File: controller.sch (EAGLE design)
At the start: 37 parts, among them IC1 7805DT, Q1 MOSFET_PCHANNEL, Q2 MOSFET-NCHANNELBSS123LT1G, Q3 MOSFET-NCHANNELFDD8780, U1 ATMEGA328P, Y1 16MHz

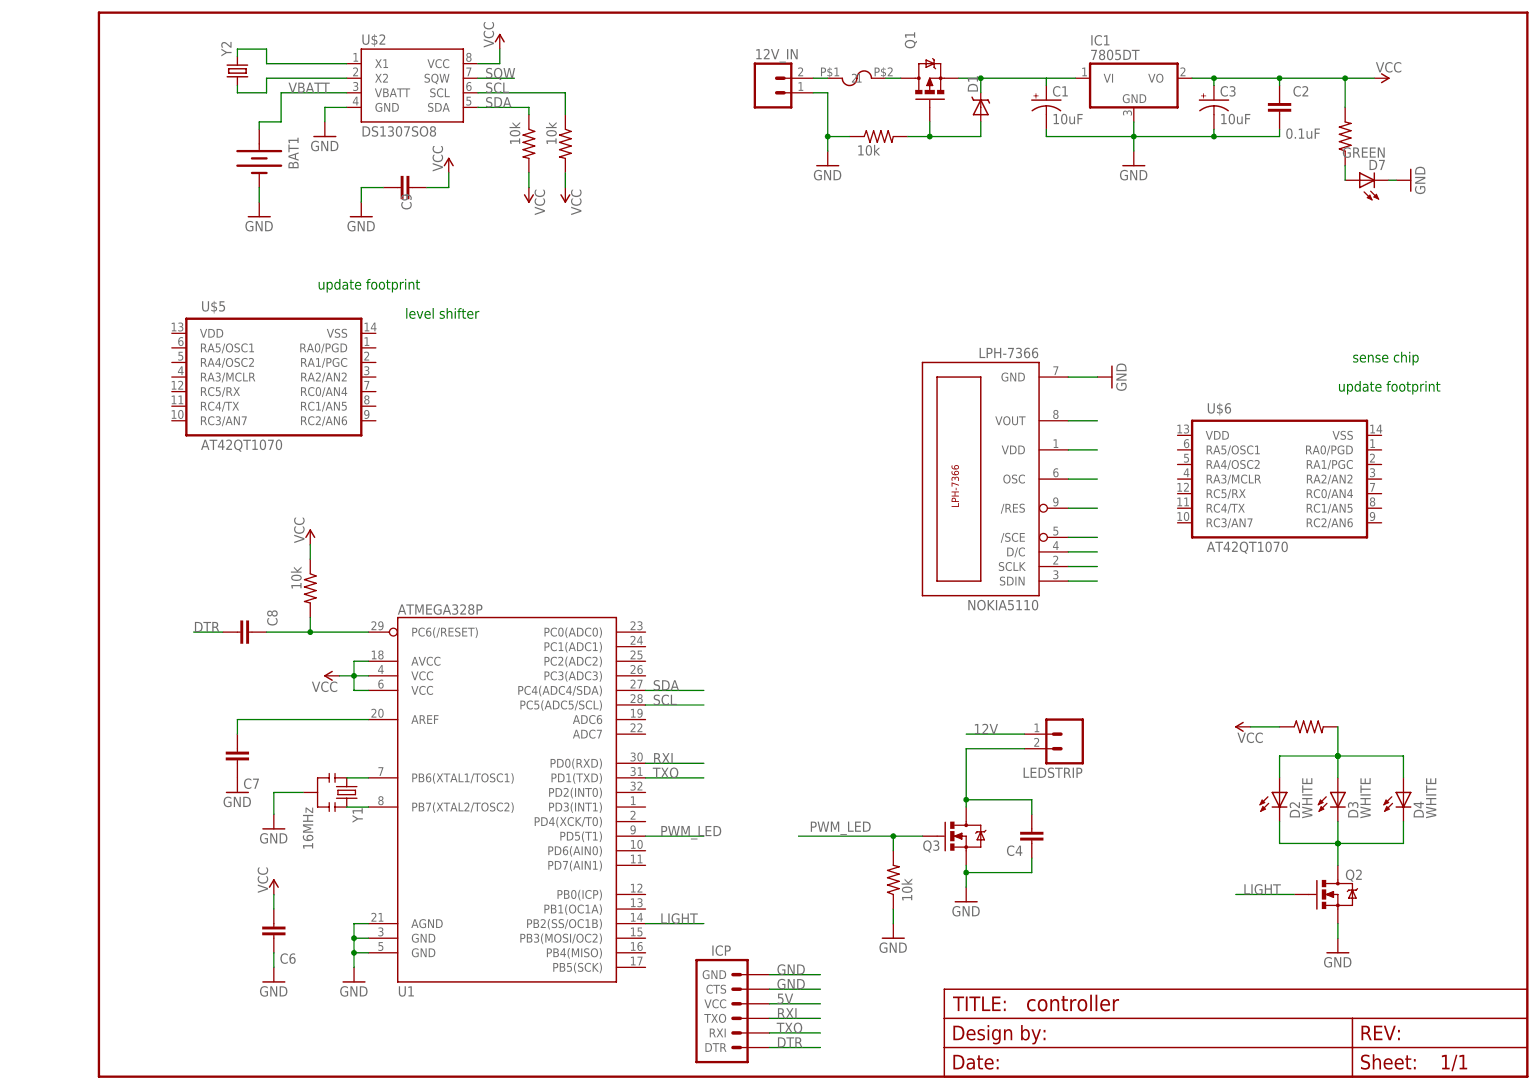
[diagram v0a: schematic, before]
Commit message: added sense IC footprint and jumper. layed out "high" power section.
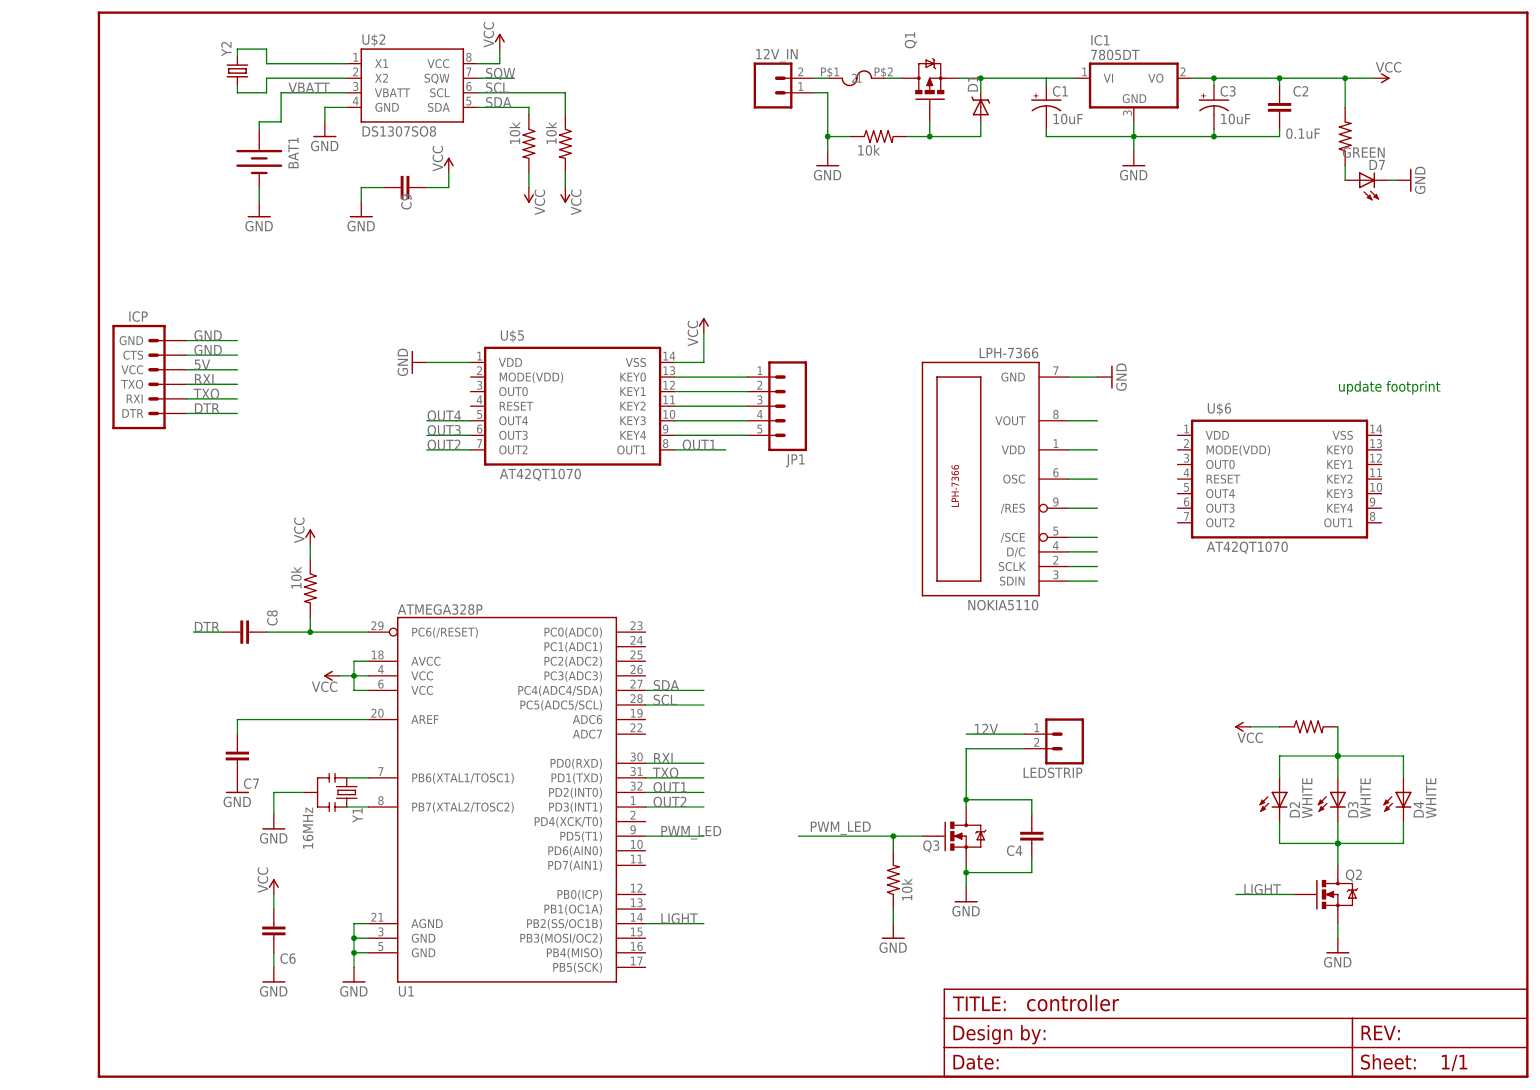
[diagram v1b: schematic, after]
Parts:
- added JP1: (no value), SparkFun-Connectors:M05PTH
- D1: value DIODE-SCHOTTKY -> DIODE-SCHOTTKYDO-214AA; device SparkFun-DiscreteSemi:DIODE-SCHOTTKY -> jt_parts:DIODE-SCHOTTKYDO-214AA
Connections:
- new net KEY4: JP1.5, U$5.KEY4
- new net N$24: JP1.4, U$5.KEY3
- new net N$25: JP1.3, U$5.KEY2
- new net N$26: JP1.2, U$5.KEY1
- new net N$27: JP1.1, U$5.KEY0
- new net OUT1: U$5.OUT1, U1.PD2(INT0)
- new net OUT2: U$5.OUT2, U1.PD3(INT1)
- new net OUT3: U$5.OUT3
- new net OUT4: U$5.OUT4
- net 5V: now also U$5.VSS
- net GND: now also U$5.VDD
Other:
- note removed: "level shifter"
- note removed: "sense chip"
- moved on the sheet: ICP, U$5, U$6
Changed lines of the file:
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@@
 <part name="GND19" library="SparkFun-Aesthetics" deviceset="GND" device=""/>
 <part name="Q1" library="jt_parts" deviceset="MOSFET_PCHANNEL" device="" value=""/>
-<part name="D1" library="SparkFun-DiscreteSemi" deviceset="DIODE-SCHOTTKY" device="" value=""/>
+<part name="D1" library="jt_parts" deviceset="DIODE-SCHOTTKY" device="DO-214AA" value=""/>
 <part name="U$17" library="jt_parts" deviceset="RESISTOR" device="" value="10k"/>
 <part name="NOKIA5110" library="lph-7366" deviceset="LPH-7366" device=""/>
@@
 <part name="U$5" library="jt_parts" deviceset="AT42QT1070" device=""/>
 <part name="U$6" library="jt_parts" deviceset="AT42QT1070" device=""/>
+<part name="SUPPLY2" library="SparkFun-Aesthetics" deviceset="VCC" device=""/>
+<part name="GND3" library="SparkFun-Aesthetics" deviceset="GND" device=""/>
+<part name="JP1" library="SparkFun-Connectors" deviceset="M05" device="PTH"/>
 </parts>
 <sheets>
@@
 <plain>
 <text x="231.14" y="228.6" size="1.778" layer="91">update footprint</text>
-<text x="53.34" y="246.38" size="1.778" layer="91">update footprint</text>
-<text x="68.58" y="241.3" size="1.778" layer="91">level shifter</text>
-<text x="233.68" y="233.68" size="1.778" layer="91">sense chip</text>
 </plain>
 <instances>
@@
 <instance part="C4" gate="G$1" x="177.8" y="152.4" rot="R180"/>
 <instance part="U1" gate="G$1" x="85.09" y="161.29"/>
-<instance part="ICP" gate="G$1" x="127" y="119.38"/>
+<instance part="ICP" gate="G$1" x="25.4" y="229.87"/>
 <instance part="U$2" gate="G$1" x="68.58" y="283.21"/>
 <instance part="Y1" gate="G$1" x="58.42" y="158.75" rot="R270"/>
@@
 <instance part="U$1" gate="G$1" x="15.24" y="109.22"/>
 <instance part="U$1" gate="G$2" x="162.56" y="109.22"/>
-<instance part="U$5" gate="G$1" x="45.72" y="231.14"/>
+<instance part="U$5" gate="G$1" x="97.79" y="226.06"/>
 <instance part="U$6" gate="G$1" x="220.98" y="213.36"/>
+<instance part="SUPPLY2" gate="1" x="120.65" y="238.76" smashed="yes">
+<attribute name="VALUE" x="119.634" y="236.474" size="1.778" layer="96" rot="R90"/>
+</instance>
+<instance part="GND3" gate="1" x="69.85" y="233.68" smashed="yes" rot="R270">
+<attribute name="VALUE" x="67.31" y="236.22" size="1.778" layer="96" rot="R270"/>
+</instance>
+<instance part="JP1" gate="G$1" x="135.89" y="226.06" rot="R180"/>
 </instances>
 <busses>
@@
 <segment>
 <pinref part="ICP" gate="G$1" pin="GND"/>
-<wire x1="132.08" y1="127" x2="140.97" y2="127" width="0.1524" layer="91"/>
-<label x="133.35" y="127" size="1.778" layer="95"/>
+<wire x1="30.48" y1="237.49" x2="39.37" y2="237.49" width="0.1524" layer="91"/>
+<label x="31.75" y="237.49" size="1.778" layer="95"/>
 </segment>
 <segment>
 <pinref part="ICP" gate="G$1" pin="CTS"/>
-<wire x1="132.08" y1="124.46" x2="140.97" y2="124.46" width="0.1524" layer="91"/>
-<label x="133.35" y="124.46" size="1.778" layer="95"/>
+<wire x1="30.48" y1="234.95" x2="39.37" y2="234.95" width="0.1524" layer="91"/>
+<label x="31.75" y="234.95" size="1.778" layer="95"/>
 </segment>
 <segment>
@@
 <wire x1="166.37" y1="144.78" x2="166.37" y2="142.24" width="0.1524" layer="91"/>
 <junction x="166.37" y="144.78"/>
+</segment>
+<segment>
+<pinref part="U$5" gate="G$1" pin="VDD"/>
+<wire x1="80.01" y1="233.68" x2="72.39" y2="233.68" width="0.1524" layer="91"/>
+<pinref part="GND3" gate="1" pin="GND"/>
 </segment>
 </net>
@@
 <segment>
 <pinref part="ICP" gate="G$1" pin="VCC"/>
-<wire x1="132.08" y1="121.92" x2="140.97" y2="121.92" width="0.1524" layer="91"/>
-<label x="133.35" y="121.92" size="1.778" layer="95"/>
+<wire x1="30.48" y1="232.41" x2="39.37" y2="232.41" width="0.1524" layer="91"/>
+<label x="31.75" y="232.41" size="1.778" layer="95"/>
 </segment>
 <segment>
@@
 <wire x1="184.15" y1="218.44" x2="189.23" y2="218.44" width="0.1524" layer="91"/>
 </segment>
+<segment>
+<pinref part="U$5" gate="G$1" pin="VSS"/>
+<wire x1="115.57" y1="233.68" x2="120.65" y2="233.68" width="0.1524" layer="91"/>
+<wire x1="120.65" y1="233.68" x2="120.65" y2="238.76" width="0.1524" layer="91"/>
+<pinref part="SUPPLY2" gate="1" pin="VCC"/>
+</segment>
 </net>
 <net name="N$1" class="0">
@@
 <segment>
 <pinref part="ICP" gate="G$1" pin="TXO"/>
-<wire x1="132.08" y1="119.38" x2="140.97" y2="119.38" width="0.1524" layer="91"/>
-<label x="133.35" y="119.38" size="1.778" layer="95"/>
+<wire x1="30.48" y1="229.87" x2="39.37" y2="229.87" width="0.1524" layer="91"/>
+<label x="31.75" y="229.87" size="1.778" layer="95"/>
 </segment>
 <segment>
@@
 <segment>
 <pinref part="ICP" gate="G$1" pin="RXI"/>
-<wire x1="132.08" y1="116.84" x2="140.97" y2="116.84" width="0.1524" layer="91"/>
-<label x="133.35" y="116.84" size="1.778" layer="95"/>
+<wire x1="30.48" y1="227.33" x2="39.37" y2="227.33" width="0.1524" layer="91"/>
+<label x="31.75" y="227.33" size="1.778" layer="95"/>
 </segment>
 <segment>
@@
 <segment>
 <pinref part="ICP" gate="G$1" pin="DTR"/>
-<wire x1="132.08" y1="114.3" x2="140.97" y2="114.3" width="0.1524" layer="91"/>
-<label x="133.35" y="114.3" size="1.778" layer="95"/>
+<wire x1="30.48" y1="224.79" x2="39.37" y2="224.79" width="0.1524" layer="91"/>
+<label x="31.75" y="224.79" size="1.778" layer="95"/>
 </segment>
 <segment>
@@
 </segment>
 </net>
+<net name="OUT3" class="0">
+<segment>
+<pinref part="U$5" gate="G$1" pin="OUT3"/>
+<wire x1="80.01" y1="220.98" x2="72.39" y2="220.98" width="0.1524" layer="91"/>
+<label x="72.39" y="220.98" size="1.778" layer="95"/>
+</segment>
+</net>
+<net name="OUT2" class="0">
+<segment>
+<pinref part="U$5" gate="G$1" pin="OUT2"/>
+<wire x1="80.01" y1="218.44" x2="72.39" y2="218.44" width="0.1524" layer="91"/>
+<label x="72.39" y="218.44" size="1.778" layer="95"/>
+</segment>
+<segment>
+<pinref part="U1" gate="G$1" pin="PD3(INT1)"/>
+<wire x1="110.49" y1="156.21" x2="120.65" y2="156.21" width="0.1524" layer="91"/>
+<label x="111.76" y="156.21" size="1.778" layer="95"/>
+</segment>
+</net>
+<net name="OUT1" class="0">
+<segment>
+<pinref part="U$5" gate="G$1" pin="OUT1"/>
+<wire x1="115.57" y1="218.44" x2="124.46" y2="218.44" width="0.1524" layer="91"/>
+<label x="116.84" y="218.44" size="1.778" layer="95"/>
+</segment>
+<segment>
+<pinref part="U1" gate="G$1" pin="PD2(INT0)"/>
+<wire x1="110.49" y1="158.75" x2="120.65" y2="158.75" width="0.1524" layer="91"/>
+<label x="111.76" y="158.75" size="1.778" layer="95"/>
+</segment>
+</net>
+<net name="KEY4" class="0">
+<segment>
+<pinref part="U$5" gate="G$1" pin="KEY4"/>
+<wire x1="115.57" y1="220.98" x2="128.27" y2="220.98" width="0.1524" layer="91"/>
+<pinref part="JP1" gate="G$1" pin="5"/>
+</segment>
+</net>
+<net name="N$24" class="0">
+<segment>
+<pinref part="U$5" gate="G$1" pin="KEY3"/>
+<wire x1="115.57" y1="223.52" x2="128.27" y2="223.52" width="0.1524" layer="91"/>
+<pinref part="JP1" gate="G$1" pin="4"/>
+</segment>
+</net>
+<net name="N$25" class="0">
+<segment>
+<pinref part="U$5" gate="G$1" pin="KEY2"/>
+<pinref part="JP1" gate="G$1" pin="3"/>
+<wire x1="115.57" y1="226.06" x2="128.27" y2="226.06" width="0.1524" layer="91"/>
+</segment>
+</net>
+<net name="N$26" class="0">
+<segment>
+<pinref part="U$5" gate="G$1" pin="KEY1"/>
+<pinref part="JP1" gate="G$1" pin="2"/>
+<wire x1="128.27" y1="228.6" x2="115.57" y2="228.6" width="0.1524" layer="91"/>
+</segment>
+</net>
+<net name="N$27" class="0">
+<segment>
+<pinref part="U$5" gate="G$1" pin="KEY0"/>
+<pinref part="JP1" gate="G$1" pin="1"/>
+<wire x1="115.57" y1="231.14" x2="128.27" y2="231.14" width="0.1524" layer="91"/>
+</segment>
+</net>
+<net name="OUT4" class="0">
+<segment>
+<wire x1="78.74" y1="223.52" x2="77.47" y2="223.52" width="0.1524" layer="91"/>
+<pinref part="U$5" gate="G$1" pin="OUT4"/>
+<wire x1="77.47" y1="223.52" x2="72.39" y2="223.52" width="0.1524" layer="91"/>
+<wire x1="78.74" y1="223.52" x2="80.01" y2="223.52" width="0.1524" layer="91"/>
+<label x="72.39" y="223.52" size="1.778" layer="95"/>
+</segment>
+</net>

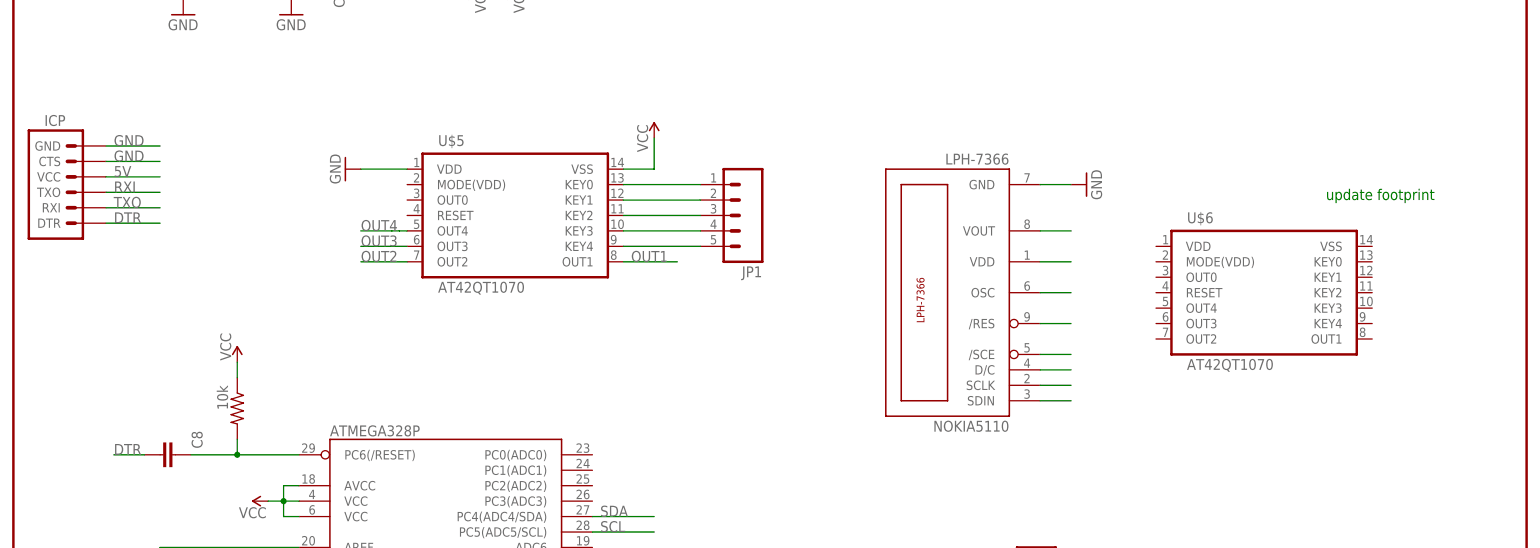
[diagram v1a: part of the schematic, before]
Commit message: made 12V traces narrower. modified nokia5110 package.
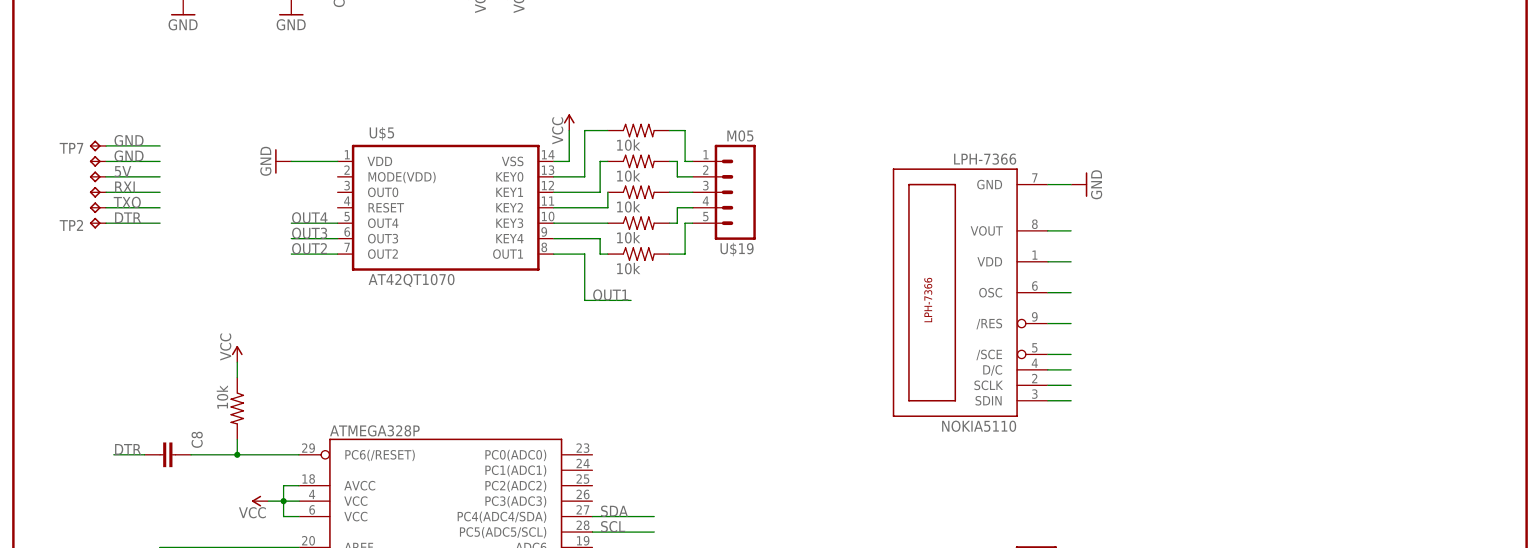
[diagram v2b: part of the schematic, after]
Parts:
- removed ICP: (no value), SparkFun-Connectors:ARDUINO_SERIAL_PROGRAMSMD
- removed JP1: (no value), SparkFun-Connectors:M05PTH
- removed U$6: AT42QT1070, jt_parts:AT42QT1070
- added TP2, TP3, TP4, TP5, TP6, TP7: TPTP12SQ, testpad:TPTP12SQ
- added U$11, U$12, U$13, U$14, U$7: 10k, jt_parts:RESISTOR
- added U$19: M05, jt_parts:M05
- NOKIA5110: device lph-7366:LPH-7366 -> jt_parts:LPH-7366
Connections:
- new net N$21: U$14.2, U$19.5
- new net N$28: U$13.2, U$19.4
- new net N$29: U$12.2, U$19.3
- new net N$30: U$11.2, U$19.2
- new net N$31: U$19.1, U$7.2
- net 5V: now also TP5.TP; no longer ICP.VCC
- net DTR: now also TP2.TP; no longer ICP.DTR
- net GND: now also TP6.TP, TP7.TP; no longer ICP.CTS, ICP.GND
- net KEY4: now also U$14.1; no longer JP1.5
- net N$24: now also U$13.1; no longer JP1.4
- net N$25: now also U$12.1; no longer JP1.3
- net N$26: now also U$11.1; no longer JP1.2
- net N$27: now also U$7.1; no longer JP1.1
- net RXI: now also TP4.TP; no longer ICP.TXO
- net TXO: now also TP3.TP; no longer ICP.RXI
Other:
- note removed: "update footprint"
- moved on the sheet: NOKIA5110, U$5
